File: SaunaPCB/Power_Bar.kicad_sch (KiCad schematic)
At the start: 52 parts, among them J201 KL3RM7.62, J202 KL3RM7.62, J203 KL3RM7.62, J204 KL2RM5.08, J205 KL3RM7.62, J206 KL3RM7.62, K201 Relais_SPDT_CO, K202 Relais_SPDT_CO, K203 Relais_SPDT_CO, K204 Relais_SPDT_CO, K205 Relais_SPDT_CO, K206 Relais_SPDT_CO, K207 Relais_SPDT_CO, U201 LHE05-20B24, U202 4N25, U203 4N25, U204 4N25

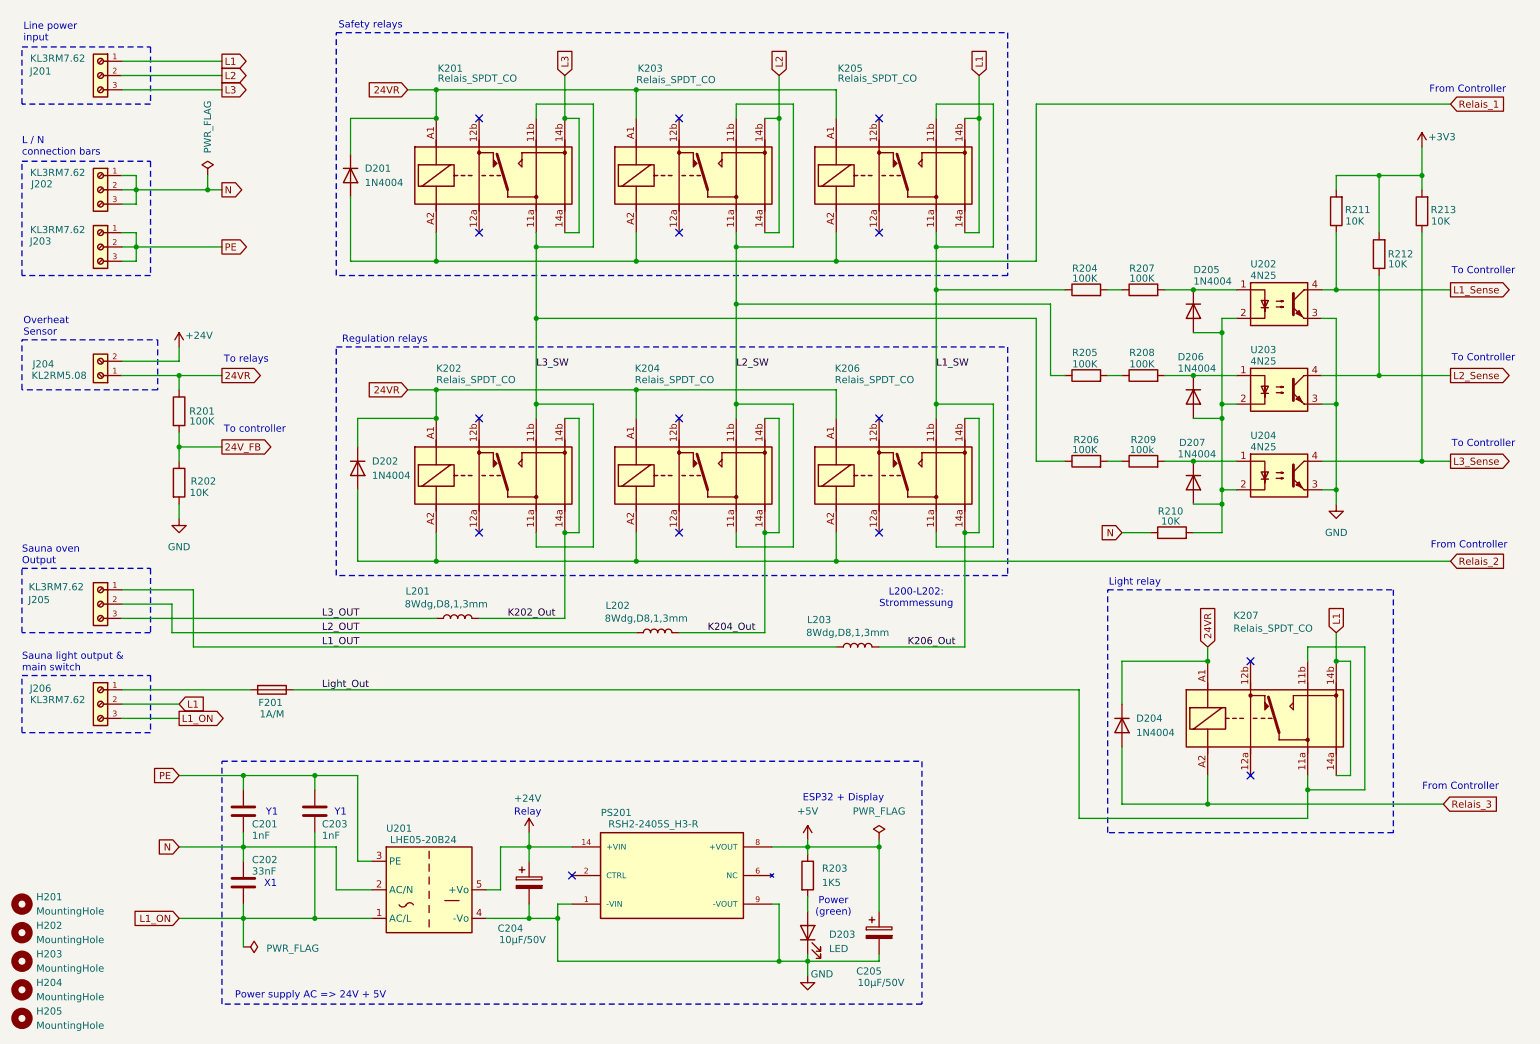
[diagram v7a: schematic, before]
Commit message: 5V regulator changed
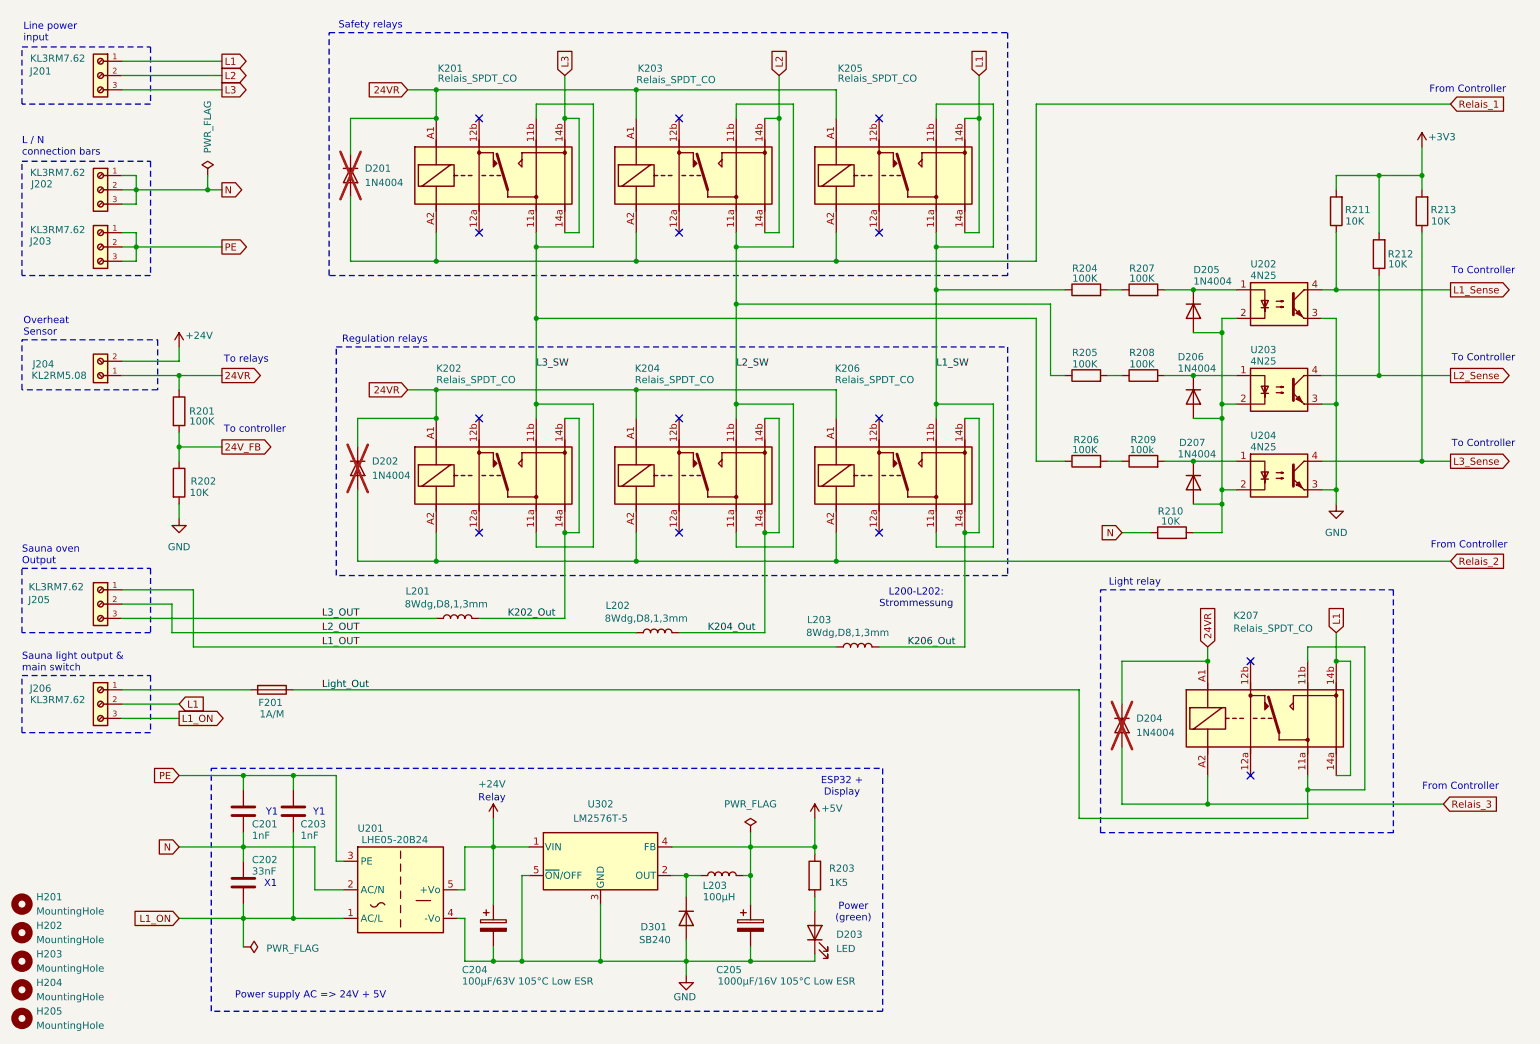
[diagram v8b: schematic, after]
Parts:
- removed PS201: RSH2-2405S_H3-R, DCDC:CONV_RSH2-2405S_H3-R, symbol DC-DC:RSH2-2405S_H3-R
- added D301: SB240, Diode_THT:D_A-405_P10.16mm_Horizontal, symbol Diode:1N4004
- added L203: 100µH, Inductor_THT:L_Radial_D7.5mm_P5.00mm_Fastron_07P, symbol Device:L
- added U302: LM2576T-5, Package_TO_SOT_THT:TO-220-5_Vertical, symbol Regulator_Switching:LM2576T-5
- C204: value 10µF/50V -> 100µF/63V 105°C Low ESR; footprint Capacitor_THT:CP_Radial_D6.3mm_P2.50mm -> Capacitor_THT:CP_Radial_D10.0mm_P5.00mm
- C205: value 10µF/50V -> 1000µF/16V 105°C Low ESR; footprint Capacitor_THT:CP_Radial_D6.3mm_P2.50mm -> Capacitor_THT:CP_Radial_D10.0mm_P5.00mm
- D201, D202, D204: now not fitted
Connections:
- net +24V: now also U302.1 (VIN)
- net +5V: now also L203.2, U302.4 (FB)
- net GND: now also D301.2 (A), U302.3 (GND), U302.5 (~{ON}/OFF)
- new net: D301.1 (K), L203.1, U302.2 (OUT)
- no-connect marks 15 -> 14
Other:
- moved on the sheet: C203, C204, C205, D203, R203, U201
